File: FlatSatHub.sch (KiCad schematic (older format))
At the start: 8 parts, among them J1 Jack-DC, SW1 SW_DIP_x03

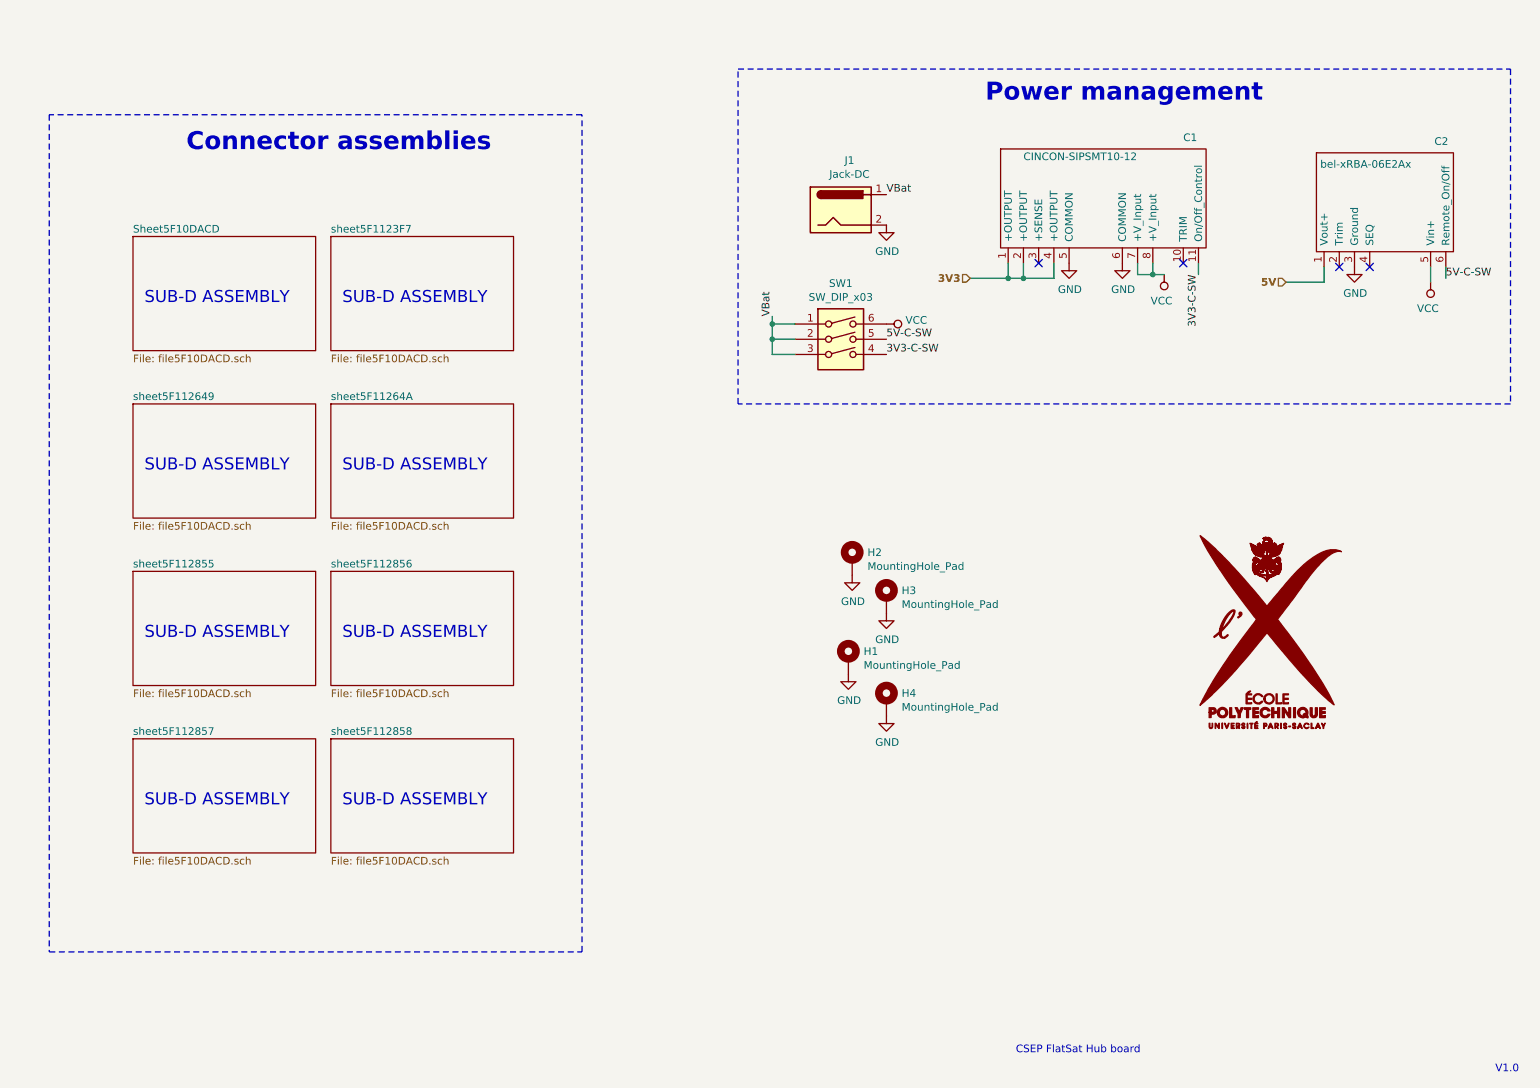
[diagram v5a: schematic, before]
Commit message: rework power management schematic
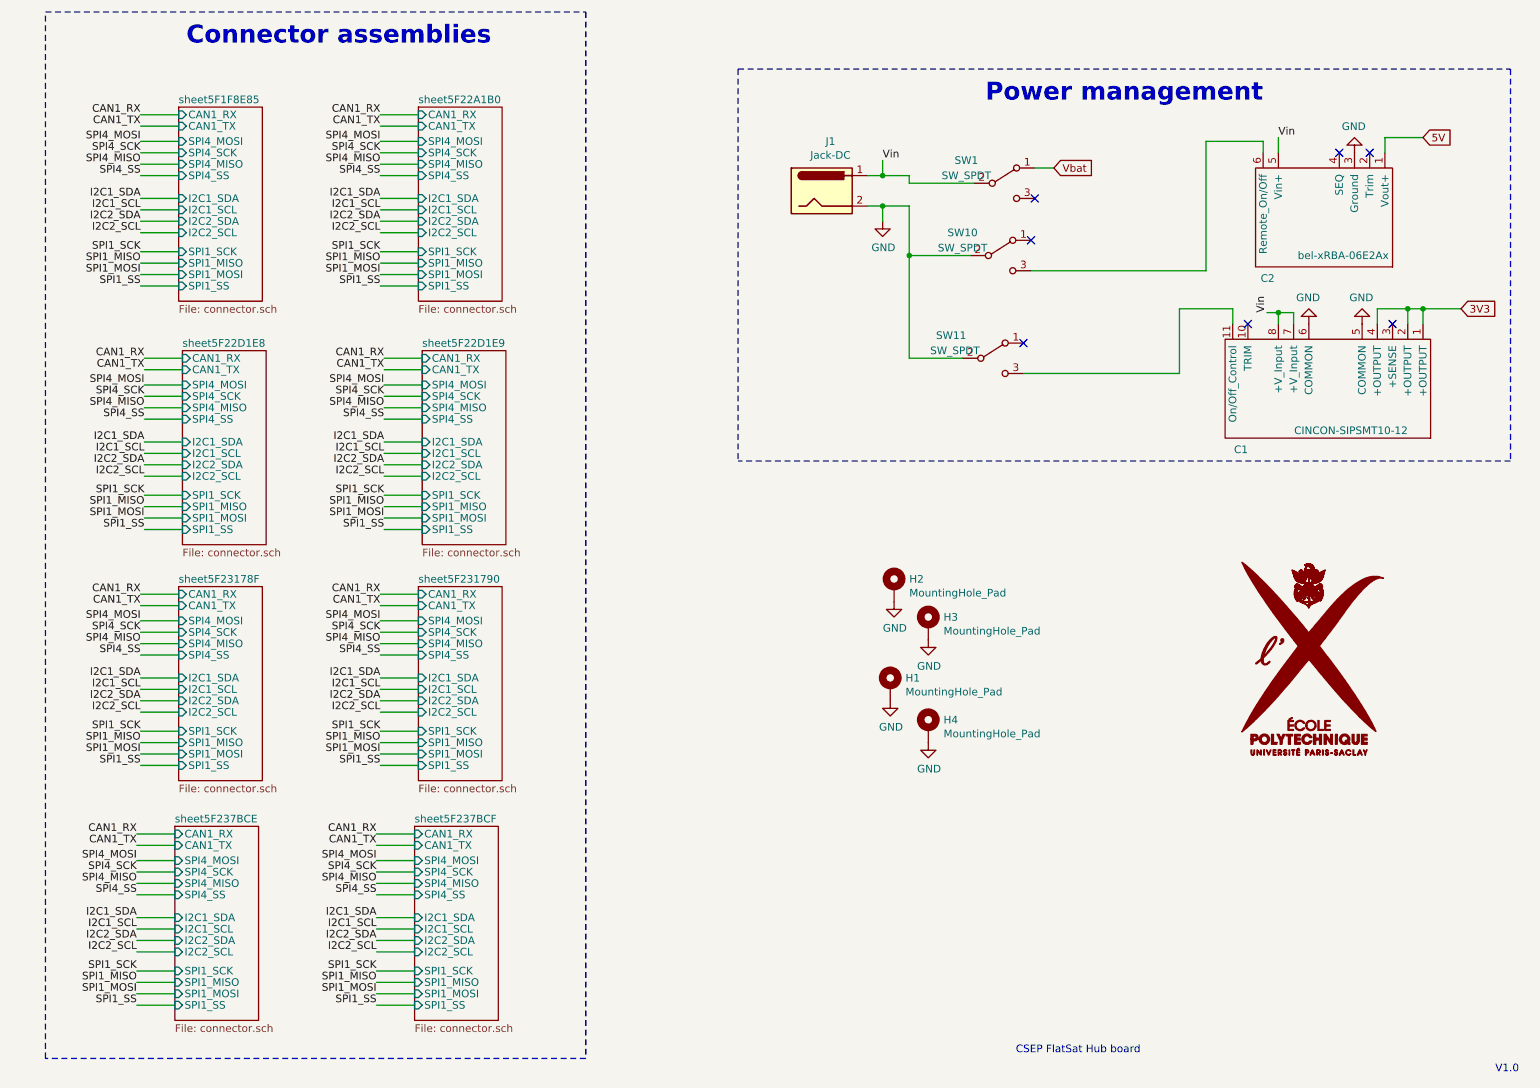
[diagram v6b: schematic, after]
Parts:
- removed SW1: SW_DIP_x03, Button_Switch_THT:SW_DIP_SPSTx03_Slide_9.78x9.8mm_W7.62mm_P2.54mm, symbol Switch:SW_DIP_x03
- added SW1, SW10, SW11: SW_SPDT, symbol Switch:SW_SPDT
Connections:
- net VCC is gone; now on net Vin: C1.7 (+V_Input), C1.8 (+V_Input), C2.5 (Vin+)
- net GND: now also SW10.2 (B), SW11.2 (B)
- net 3V3-C-SW: no longer names the net of C1.11 (On/Off_Control)
- net 3V3-C-SW: now also SW11.3 (C)
- net 5V-C-SW: no longer names the net of C2.6 (Remote_On/Off)
- net 5V-C-SW: now also SW10.3 (C)
- net VBat renamed Vin
- net Vin: now also SW1.2 (B)
- new net Vbat: SW1.1 (A)
- no-connect marks 4 -> 7
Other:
- note removed: "SUB-D ASSEMBLY"
- moved on the sheet: C1, C2, H1, H2, H3, H4

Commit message: try improving positionning
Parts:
- SW1, SW10, SW11: footprint (none) -> Button_Switch_SMD:SW_SPDT_PCM12
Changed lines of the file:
@@
 F 0 "SW1" H 7100 1925 50  0000 C CNN
 F 1 "SW_SPDT" H 7100 1825 50  0000 C CNN
-F 2 "" H 7350 1775 50  0001 C CNN
+F 2 "Button_Switch_SMD:SW_SPDT_PCM12" H 7350 1775 50  0001 C CNN
 F 3 "~" H 7350 1775 50  0001 C CNN
 	1    7350 1775
@@
 F 0 "SW10" H 7075 2400 50  0000 C CNN
 F 1 "SW_SPDT" H 7075 2300 50  0000 C CNN
-F 2 "" H 7325 2250 50  0001 C CNN
+F 2 "Button_Switch_SMD:SW_SPDT_PCM12" H 7325 2250 50  0001 C CNN
 F 3 "~" H 7325 2250 50  0001 C CNN
 	1    7325 2250
@@
 F 0 "SW11" H 7000 3075 50  0000 C CNN
 F 1 "SW_SPDT" H 7025 2975 50  0000 C CNN
-F 2 "" H 7275 2925 50  0001 C CNN
+F 2 "Button_Switch_SMD:SW_SPDT_PCM12" H 7275 2925 50  0001 C CNN
 F 3 "~" H 7275 2925 50  0001 C CNN
 	1    7275 2925

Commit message: minor improvements
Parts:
- removed SW1, SW10, SW11: SW_SPDT, Button_Switch_SMD:SW_SPDT_PCM12, symbol Switch:SW_SPDT
- added D? (x3): LED, symbol Device:LED
- added R? (x3): R, symbol Device:R
- added SW1: SW_DIP_x02, Button_Switch_THT:SW_DIP_SPSTx02_Slide_6.7x6.64mm_W7.62mm_P2.54mm_LowProfile, symbol Switch:SW_DIP_x02
- added SW10: SW_SPST, Button_Switch_THT:SW_DIP_SPSTx01_Slide_9.78x4.72mm_W7.62mm_P2.54mm, symbol Switch:SW_SPST
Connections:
- net GND: now also R?.1, R?.1, R?.1, SW1.1, SW1.2
- net Vbat: now also D?.2 (A), SW10.2 (B)
- net Vin: now also SW10.1 (A)
- net at C2.6 (Remote_On/Off): now also D?.2 (A), SW1.4
- net at C1.11 (On/Off_Control): now also D?.2 (A), SW1.3
- new net: D?.1 (K), R?.2 (x3)
- no-connect marks 7 -> 4
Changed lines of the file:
@@
 	1    0    0    -1
 $EndComp
-Text GLabel 7675 1675 2    50   Input ~ 0
+Text GLabel 7675 1775 2    50   Input ~ 0
 Vbat
 Wire Wire Line
@@
 Wire Wire Line
 	6550 2025 6550 1925
-$Comp
-L Switch:SW_SPDT SW1
-U 1 1 5F58DCCA
-P 7350 1775
-F 0 "SW1" H 7100 1925 50  0000 C CNN
-F 1 "SW_SPDT" H 7100 1825 50  0000 C CNN
-F 2 "Button_Switch_SMD:SW_SPDT_PCM12" H 7350 1775 50  0001 C CNN
-F 3 "~" H 7350 1775 50  0001 C CNN
-	1    7350 1775
-	1    0    0    -1
-$EndComp
-$Comp
-L Switch:SW_SPDT SW10
-U 1 1 5F5A32D7
-P 7325 2250
-F 0 "SW10" H 7075 2400 50  0000 C CNN
-F 1 "SW_SPDT" H 7075 2300 50  0000 C CNN
-F 2 "Button_Switch_SMD:SW_SPDT_PCM12" H 7325 2250 50  0001 C CNN
-F 3 "~" H 7325 2250 50  0001 C CNN
-	1    7325 2250
-	1    0    0    -1
-$EndComp
-$Comp
-L Switch:SW_SPDT SW11
-U 1 1 5F5AC906
-P 7275 2925
-F 0 "SW11" H 7000 3075 50  0000 C CNN
-F 1 "SW_SPDT" H 7025 2975 50  0000 C CNN
-F 2 "Button_Switch_SMD:SW_SPDT_PCM12" H 7275 2925 50  0001 C CNN
-F 3 "~" H 7275 2925 50  0001 C CNN
-	1    7275 2925
-	1    0    0    -1
-$EndComp
 Wire Wire Line
 	6725 1775 7150 1775
@@
 Vin
 Wire Wire Line
-	7675 1675 7550 1675
-NoConn ~ 7550 1875
+	7675 1775 7600 1775
 Wire Wire Line
-	6725 2250 7125 2250
-Wire Wire Line
-	6725 2925 7075 2925
-Wire Wire Line
-	6725 2250 6725 2925
-Wire Wire Line
-	7525 2350 8675 2350
-Wire Wire Line
-	7475 3025 8500 3025
-Wire Wire Line
-	8500 3025 8500 2600
-Wire Wire Line
-	8500 2600 8850 2600
-Wire Wire Line
-	8850 2600 8850 2700
+	7525 2350 7600 2350
 Wire Wire Line
 	8675 1500 9050 1500
@@
 Wire Wire Line
 	8675 1500 8675 2350
-NoConn ~ 7525 2150
-NoConn ~ 7475 2825
 NoConn ~ 8950 2700
 Wire Wire Line
 	6550 1925 6725 1925
-Wire Wire Line
-	6725 1925 6725 2250
 Connection ~ 6550 1925
-Connection ~ 6725 2250
 Connection ~ 6550 1725
 Wire Wire Line
 	6550 1725 6725 1725
+$Comp
+L Switch:SW_DIP_x02 SW1
+U 1 1 5F225365
+P 7225 2450
+F 0 "SW1" H 7225 2817 50  0000 C CNN
+F 1 "SW_DIP_x02" H 7225 2726 50  0000 C CNN
+F 2 "Button_Switch_THT:SW_DIP_SPSTx02_Slide_6.7x6.64mm_W7.62mm_P2.54mm_LowProfile" H 7225 2450 50  0001 C CNN
+F 3 "~" H 7225 2450 50  0001 C CNN
+	1    7225 2450
+	1    0    0    -1
+$EndComp
+Wire Wire Line
+	8850 2450 7600 2450
+Wire Wire Line
+	8850 2450 8850 2700
+Wire Wire Line
+	6925 2450 6725 2450
+Wire Wire Line
+	6725 2450 6725 2350
+Wire Wire Line
+	6925 2350 6725 2350
+Connection ~ 6725 2350
+Wire Wire Line
+	6725 2350 6725 1925
+$Comp
+L Switch:SW_SPST SW10
+U 1 1 5F2B7346
+P 7350 1775
+F 0 "SW10" H 7350 2010 50  0000 C CNN
+F 1 "SW_SPST" H 7350 1919 50  0000 C CNN
+F 2 "Button_Switch_THT:SW_DIP_SPSTx01_Slide_9.78x4.72mm_W7.62mm_P2.54mm" H 7350 1775 50  0001 C CNN
+F 3 "~" H 7350 1775 50  0001 C CNN
+	1    7350 1775
+	1    0    0    -1
+$EndComp
+$Comp
+L Device:LED D?
+U 1 1 5F2D3A02
+P 7850 1600
+F 0 "D?" H 7843 1345 50  0000 C CNN
+F 1 "LED" H 7843 1436 50  0000 C CNN
+F 2 "" H 7850 1600 50  0001 C CNN
+F 3 "~" H 7850 1600 50  0001 C CNN
+	1    7850 1600
+	-1   0    0    1
+$EndComp
+$Comp
+L Device:LED D?
+U 1 1 5F2D4A24
+P 7825 2250
+F 0 "D?" H 7818 1995 50  0000 C CNN
+F 1 "LED" H 7818 2086 50  0000 C CNN
+F 2 "" H 7825 2250 50  0001 C CNN
+F 3 "~" H 7825 2250 50  0001 C CNN
+	1    7825 2250
+	-1   0    0    1
+$EndComp
+$Comp
+L Device:LED D?
+U 1 1 5F2DEAA8
+P 7825 2575
+F 0 "D?" H 7818 2320 50  0000 C CNN
+F 1 "LED" H 7818 2411 50  0000 C CNN
+F 2 "" H 7825 2575 50  0001 C CNN
+F 3 "~" H 7825 2575 50  0001 C CNN
+	1    7825 2575
+	-1   0    0    1
+$EndComp
+$Comp
+L Device:R R?
+U 1 1 5F2E82E2
+P 8150 1600
+F 0 "R?" V 7943 1600 50  0000 C CNN
+F 1 "R" V 8034 1600 50  0000 C CNN
+F 2 "" V 8080 1600 50  0001 C CNN
+F 3 "~" H 8150 1600 50  0001 C CNN
+	1    8150 1600
+	0    1    1    0
+$EndComp
+$Comp
+L Device:R R?
+U 1 1 5F2E9255
+P 8125 2250
+F 0 "R?" V 7918 2250 50  0000 C CNN
+F 1 "R" V 8009 2250 50  0000 C CNN
+F 2 "" V 8055 2250 50  0001 C CNN
+F 3 "~" H 8125 2250 50  0001 C CNN
+	1    8125 2250
+	0    1    1    0
+$EndComp
+$Comp
+L Device:R R?
+U 1 1 5F2F2A98
+P 8125 2575
+F 0 "R?" V 7918 2575 50  0000 C CNN
+F 1 "R" V 8009 2575 50  0000 C CNN
+F 2 "" V 8055 2575 50  0001 C CNN
+F 3 "~" H 8125 2575 50  0001 C CNN
+	1    8125 2575
+	0    1    1    0
+$EndComp
+$Comp
+L power:GND #PWR?
+U 1 1 5F2FC3AF
+P 8300 1600
+F 0 "#PWR?" H 8300 1350 50  0001 C CNN
+F 1 "GND" V 8305 1472 50  0000 R CNN
+F 2 "" H 8300 1600 50  0001 C CNN
+F 3 "" H 8300 1600 50  0001 C CNN
+	1    8300 1600
+	0    -1   -1   0
+$EndComp
+$Comp
+L power:GND #PWR?
+U 1 1 5F2FCCF0
+P 8275 2250
+F 0 "#PWR?" H 8275 2000 50  0001 C CNN
+F 1 "GND" V 8280 2122 50  0000 R CNN
+F 2 "" H 8275 2250 50  0001 C CNN
+F 3 "" H 8275 2250 50  0001 C CNN
+	1    8275 2250
+	0    -1   -1   0
+$EndComp
+$Comp
+L power:GND #PWR?
+U 1 1 5F3063BD
+P 8275 2575
+F 0 "#PWR?" H 8275 2325 50  0001 C CNN
+F 1 "GND" V 8280 2447 50  0000 R CNN
+F 2 "" H 8275 2575 50  0001 C CNN
+F 3 "" H 8275 2575 50  0001 C CNN
+	1    8275 2575
+	0    -1   -1   0
+$EndComp
+Wire Wire Line
+	7700 1600 7600 1600
+Wire Wire Line
+	7600 1600 7600 1775
+Connection ~ 7600 1775
+Wire Wire Line
+	7600 1775 7550 1775
+Wire Wire Line
+	7675 2250 7600 2250
+Wire Wire Line
+	7600 2250 7600 2350
+Connection ~ 7600 2350
+Wire Wire Line
+	7600 2350 8675 2350
+Wire Wire Line
+	7675 2575 7600 2575
+Wire Wire Line
+	7600 2575 7600 2450
+Connection ~ 7600 2450
+Wire Wire Line
+	7600 2450 7525 2450
 $EndSCHEMATC
